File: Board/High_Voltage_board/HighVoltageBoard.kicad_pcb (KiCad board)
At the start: 2 copper layers, 76.2 x 36.1 mm, 24 parts, among them J2 Conn_01x03_Female, J3 Conn_01x01_MountingPin, J4 Conn_01x01_MountingPin, J5 Conn_01x01_MountingPin, J6 Conn_01x01_MountingPin, U1 LT8304-1, U2 750315839

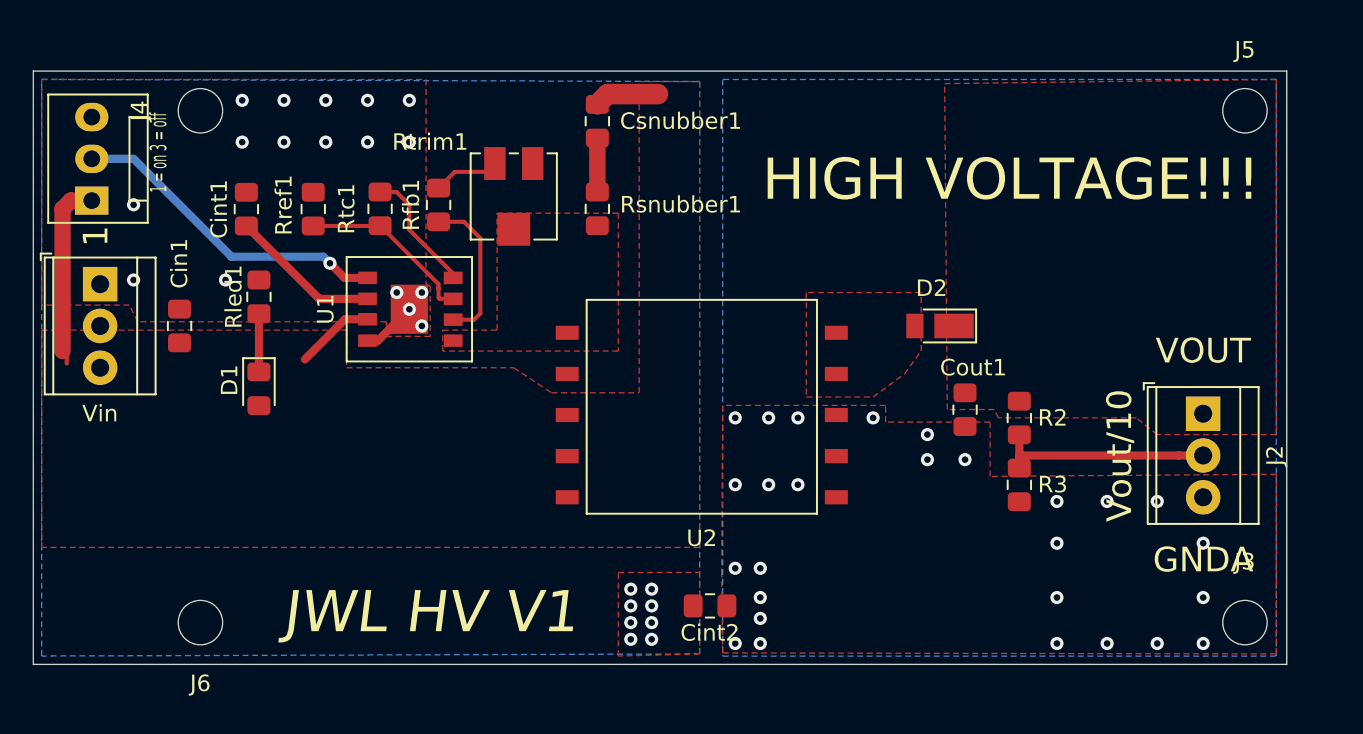
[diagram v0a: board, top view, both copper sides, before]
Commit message: updated board
fixed courty yard issue on pin
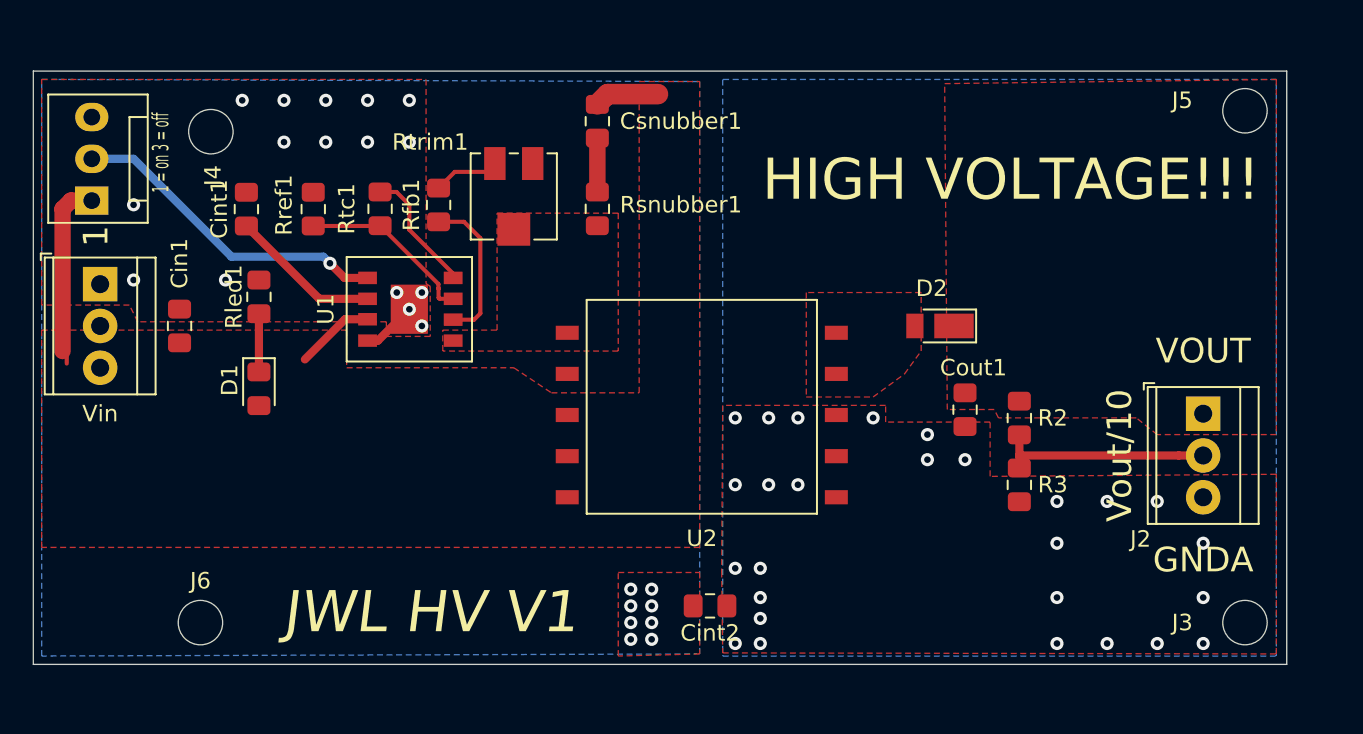
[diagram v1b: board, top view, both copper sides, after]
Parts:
- moved J4 1.42 mm to (112.4, 84.5)
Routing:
- net GND: vias 25 -> 24
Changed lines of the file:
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@@
     (thickness 1.6)
     (drawings 16)
-    (tracks 102)
+    (tracks 101)
     (zones 0)
     (modules 24)
@@
     (45 Margin user)
     (46 B.CrtYd user)
-    (47 F.CrtYd user hide)
+    (47 F.CrtYd user)
     (48 B.Fab user)
     (49 F.Fab user hide)
   )
   (setup
-    (last_trace_width 1)
+    (last_trace_width 0.25)
     (user_trace_width 0.5)
     (user_trace_width 0.75)
@@
     (descr "Terminal Block TE 282834-3, 3 pins, pitch 2.54mm, size 8.08x6.5mm^2, drill diamater 1.1mm, pad diameter 2.1mm, see http://www.te.com/commerce/DocumentDelivery/DDEController?Action=showdoc&DocId=Customer+Drawing%7F282834%7FC1%7Fpdf%7FEnglish%7FENG_CD_282834_C1.pdf, script-generated using https://github.com/pointhi/kicad-footprint-generator/scripts/TerminalBlock_TE-Connectivity")
     (tags "THT Terminal Block TE 282834-3 pitch 2.54mm size 8.08x6.5mm^2 drill 1.1mm pad 2.1mm")
-    (fp_text reference J2 (at 2.54 -4.37 90) (layer F.SilkS)
+    (fp_text reference J2 (at 7.62 3.81 180) (layer F.SilkS)
       (effects (font (size 1 1) (thickness 0.15)))
     )
@@
     (descr "3-pin CPU fan Through hole pin header, see http://www.formfactors.org/developer%5Cspecs%5Crev1_2_public.pdf")
     (tags "pin header 3-pin CPU fan")
-    (fp_text reference "1 = on 3 = off" (at 2.921 4.064 270) (layer F.SilkS)
+    (fp_text reference "1 = on 3 = off" (at 2.921 4.191 270) (layer F.SilkS)
       (effects (font (size 1 0.5) (thickness 0.125)))
     )
@@
     (tags "mounting hole 2.7mm no annular")
     (attr virtual)
-    (fp_text reference J3 (at 0 -3.7) (layer F.SilkS)
+    (fp_text reference J3 (at -3.81 0) (layer F.SilkS)
       (effects (font (size 1 1) (thickness 0.15)))
     )
@@
   )
   (module MountingHole:MountingHole_2.7mm (layer F.Cu)
-    (at 111.76 83.185 90)
+    (at 112.395 84.455 90)
     (descr "Mounting Hole 2.7mm, no annular")
     (tags "mounting hole 2.7mm no annular")
     (attr virtual)
-    (fp_text reference J4 (at 0 -3.7 90) (layer F.SilkS)
+    (fp_text reference J4 (at -2.667 0.127 90) (layer F.SilkS)
       (effects (font (size 1 1) (thickness 0.15)))
     )
@@
     (tags "mounting hole 2.7mm no annular")
     (attr virtual)
-    (fp_text reference J5 (at 0 -3.7) (layer F.SilkS)
+    (fp_text reference J5 (at -3.81 -0.635) (layer F.SilkS)
       (effects (font (size 1 1) (thickness 0.15)))
     )
@@
     (tags "mounting hole 2.7mm no annular")
     (attr virtual)
-    (fp_text reference J6 (at 0 -3.7) (layer F.SilkS)
+    (fp_text reference J6 (at 0 2.54) (layer F.SilkS)
       (effects (font (size 1 1) (thickness 0.15)))
     )
@@
   (via (at 116.84 82.55) (size 0.8) (drill 0.4) (layers F.Cu B.Cu) (net 1))
   (via (at 114.3 82.55) (size 0.8) (drill 0.4) (layers F.Cu B.Cu) (net 1))
-  (via (at 114.3 85.09) (size 0.8) (drill 0.4) (layers F.Cu B.Cu) (net 1))
   (via (at 116.84 85.09) (size 0.8) (drill 0.4) (layers F.Cu B.Cu) (net 1))
   (via (at 119.38 85.09) (size 0.8) (drill 0.4) (layers F.Cu B.Cu) (net 1))
